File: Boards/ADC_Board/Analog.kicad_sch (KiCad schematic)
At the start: 81 parts, among them J13 Load Cell A, J14 Load Cell B, J15 MIPA_A, J16 Load Cell C, J17 MIPA_B, J18 Thermocouple A, J19 MIPA_C, J20 Thermocouple B, J21 Thermocouple C, J22 Cold Juntion Thermistor, U5 ADS124S08IRHBR

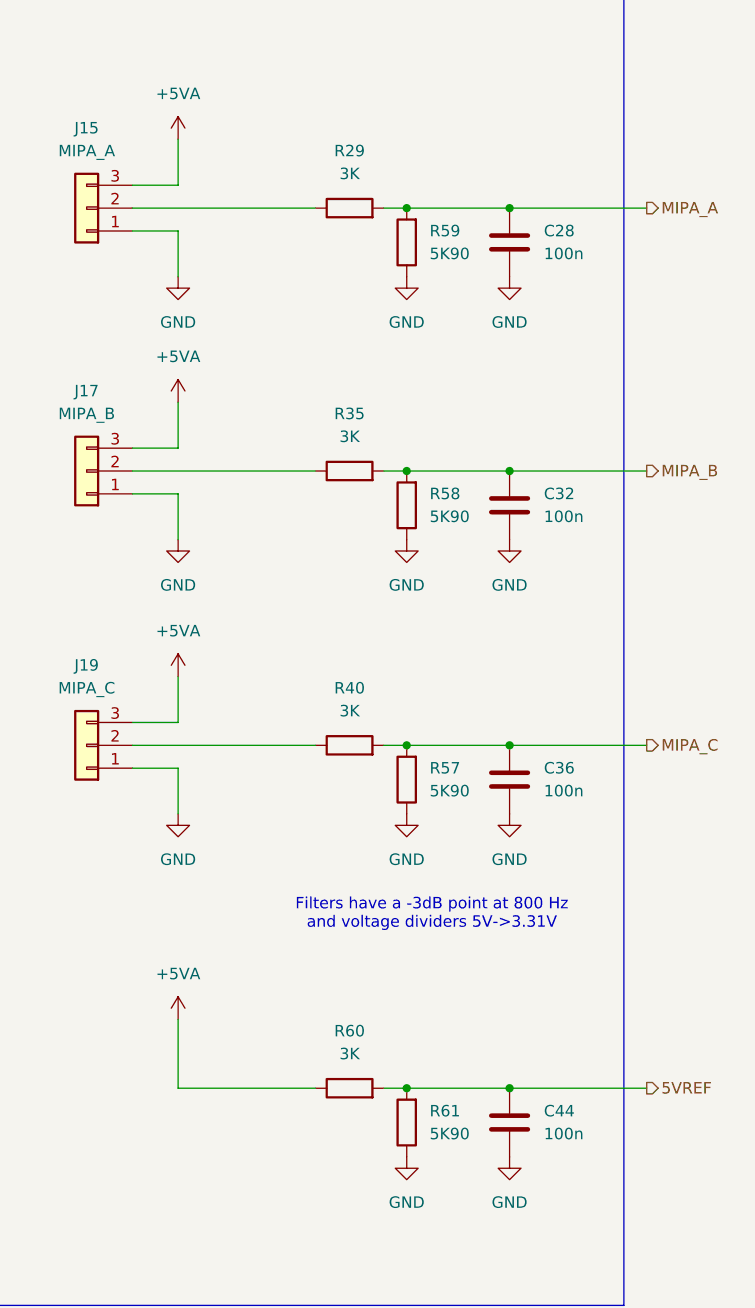
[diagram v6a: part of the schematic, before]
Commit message: Some PCB changes after ADC assembly
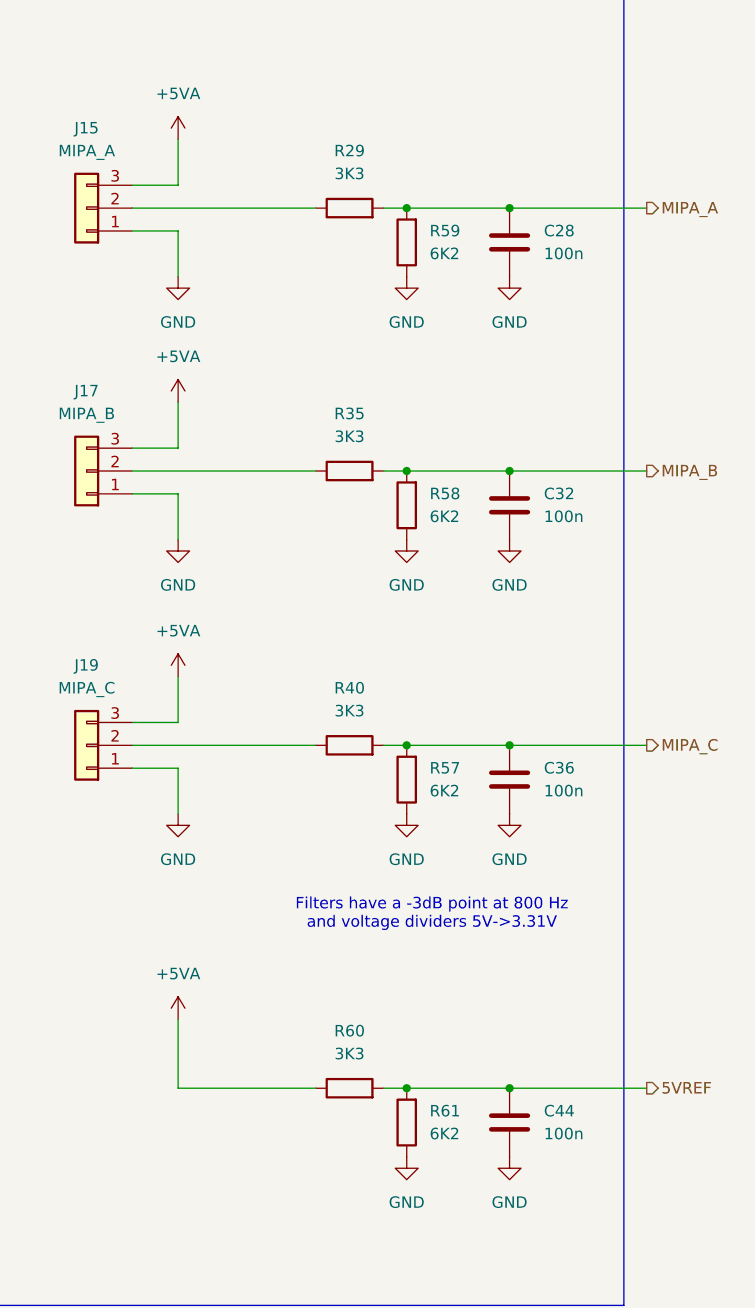
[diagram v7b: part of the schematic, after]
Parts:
- R29, R35, R40, R60: value 3K -> 3K3
- R57, R58, R59, R61: value 5K90 -> 6K2
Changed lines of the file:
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@@
 			)
 		)
-		(property "Value" "3K"
+		(property "Value" "3K3"
 			(at 354.33 143.51 90)
 			(effects
@@
 			)
 		)
-		(property "Value" "3K"
+		(property "Value" "3K3"
 			(at 354.33 212.09 90)
 			(effects
@@
 			)
 		)
-		(property "Value" "5K90"
+		(property "Value" "6K2"
 			(at 363.22 123.1899 0)
 			(effects
@@
 			)
 		)
-		(property "Value" "3K"
+		(property "Value" "3K3"
 			(at 354.33 114.3 90)
 			(effects
@@
 			)
 		)
-		(property "Value" "5K90"
+		(property "Value" "6K2"
 			(at 363.22 182.8799 0)
 			(effects
@@
 			)
 		)
-		(property "Value" "3K"
+		(property "Value" "3K3"
 			(at 354.33 173.99 90)
 			(effects
@@
 			)
 		)
-		(property "Value" "5K90"
+		(property "Value" "6K2"
 			(at 363.22 152.3999 0)
 			(effects
@@
 			)
 		)
-		(property "Value" "5K90"
+		(property "Value" "6K2"
 			(at 363.22 220.9799 0)
 			(effects
